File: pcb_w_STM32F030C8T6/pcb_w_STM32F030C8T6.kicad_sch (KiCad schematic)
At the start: 29 parts

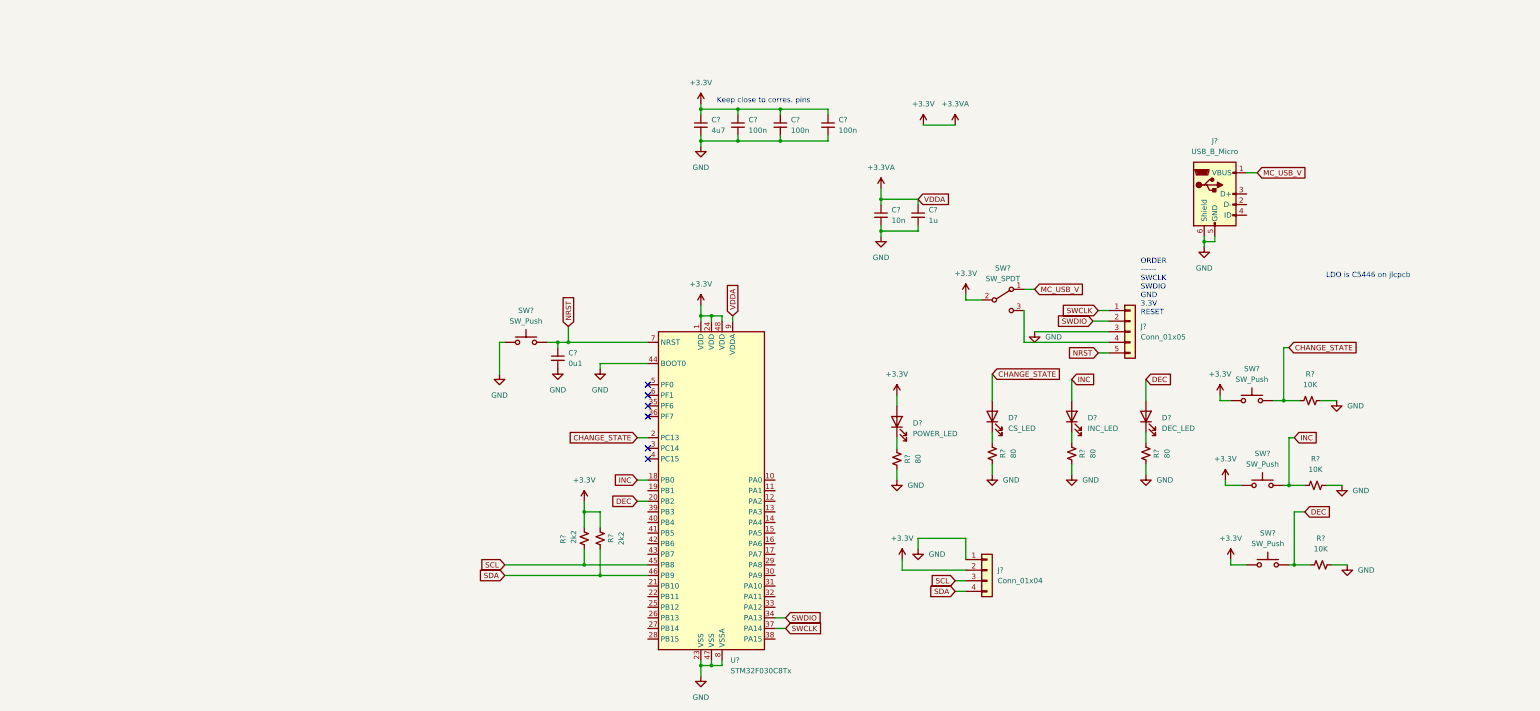
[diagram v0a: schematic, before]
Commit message: added ldo...created some footprints...and currently doing routing
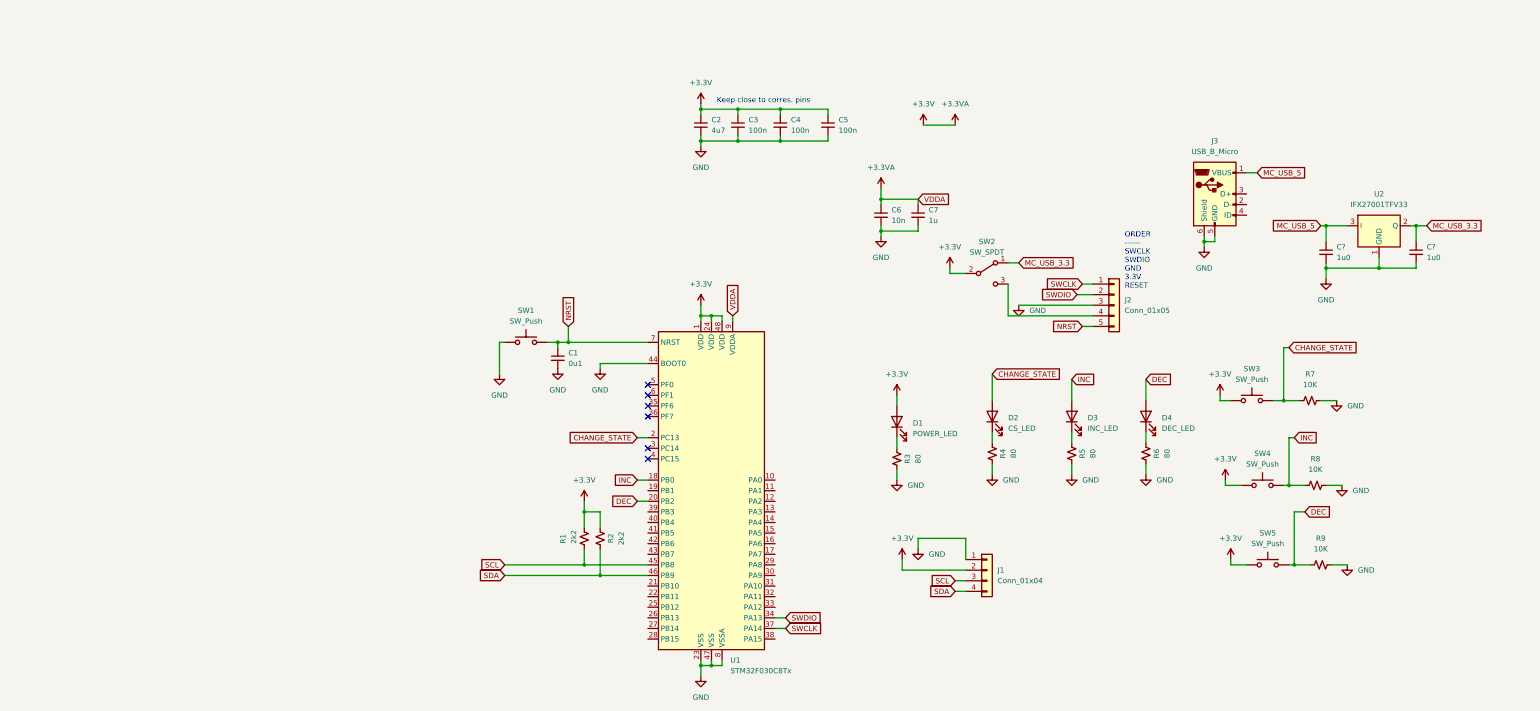
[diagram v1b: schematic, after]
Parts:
- added C? (x2): 1u0, Capacitor_SMD:C_0805_2012Metric, symbol Device:C_Small
- added U2: IFX27001TFV33, MyLibrary:SOT-23-3L, symbol Regulator_Linear:IFX27001TFV33
- J1: renamed from J?; DigiKey Part # (none) -> SSW-104-06-T-S-LL
- J2: renamed from J?; JLCPCB Part # (none) -> C124379
- SW1, SW3, SW4, SW5: renamed from SW?; footprint create one -> MyLibrary:SMD_3×4×2.0
- SW2: renamed from SW?; footprint create one -> MyLibrary:SW-SMD-JLC-C405952
- gave numbers to parts that had none: 22
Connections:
- net GND: now also C?.2, C?.2, U2.1 (GND)
- net MC_USB_V renamed MC_USB_3.3
- net MC_USB_3.3: now also C?.1, U2.2 (Q); no longer J3.1 (VBUS)
- new net MC_USB_5: C?.1, J3.1 (VBUS), U2.3 (I)
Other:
- note removed: "LDO is C5446 on jlcpcb"
- moved on the sheet: J2, SW2

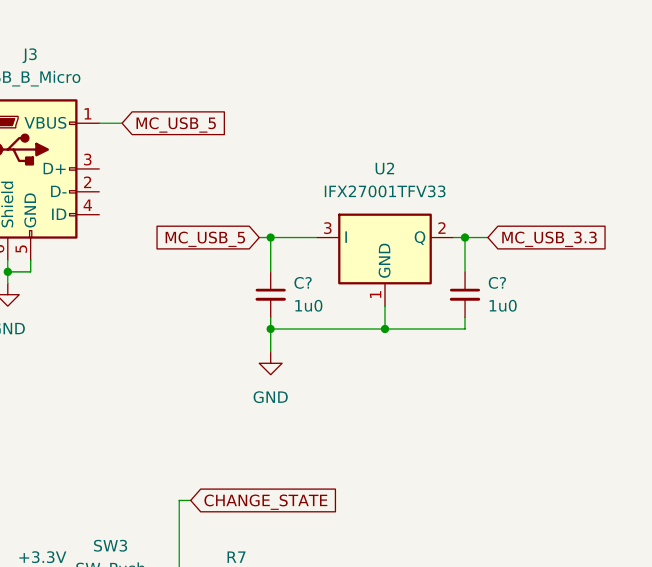
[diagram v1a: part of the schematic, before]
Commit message: made board 4 layers
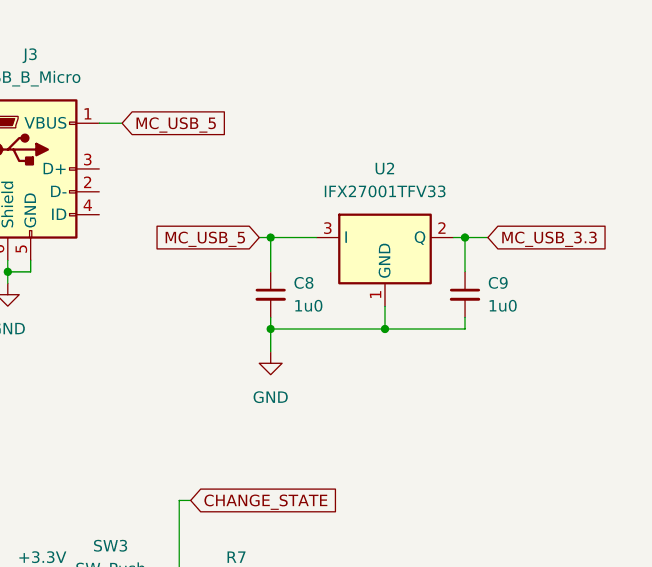
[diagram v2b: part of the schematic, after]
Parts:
- C1: footprint Capacitor_SMD:C_01005_0402Metric -> Capacitor_SMD:C_0805_2012Metric; DigiKey Part # GRM02YR60J104ME01L -> 0805ZC104KAT2A
- gave numbers to parts that had none: 2
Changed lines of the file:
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@@
       (effects (font (size 1.27 1.27)) (justify left))
     )
-    (property "Footprint" "Capacitor_SMD:C_01005_0402Metric" (id 2) (at 52.07 92.71 0)
+    (property "Footprint" "Capacitor_SMD:C_0805_2012Metric" (id 2) (at 52.07 92.71 0)
       (effects (font (size 1.27 1.27)) hide)
     )
@@
       (effects (font (size 1.27 1.27)) hide)
     )
-    (property "DigiKey Part #" "GRM02YR60J104ME01L" (id 5) (at 52.07 92.71 0)
+    (property "DigiKey Part #" "0805ZC104KAT2A" (id 5) (at 52.07 92.71 0)
       (effects (font (size 1.27 1.27)) hide)
     )
@@
   (symbol (lib_id "power:GND") (at 236.22 73.66 0) (unit 1)
     (in_bom yes) (on_board yes) (fields_autoplaced)
-    (property "Reference" "#PWR?" (id 0) (at 236.22 80.01 0)
+    (property "Reference" "#PWR0129" (id 0) (at 236.22 80.01 0)
       (effects (font (size 1.27 1.27)) hide)
     )
@@
   (symbol (lib_id "Device:C_Small") (at 257.81 67.31 0) (unit 1)
     (in_bom yes) (on_board yes) (fields_autoplaced)
-    (property "Reference" "C?" (id 0) (at 260.35 66.0462 0)
+    (property "Reference" "C9" (id 0) (at 260.35 66.0462 0)
       (effects (font (size 1.27 1.27)) (justify left))
     )
@@
   (symbol (lib_id "Device:C_Small") (at 236.22 67.31 0) (unit 1)
     (in_bom yes) (on_board yes) (fields_autoplaced)
-    (property "Reference" "C?" (id 0) (at 238.76 66.0462 0)
+    (property "Reference" "C8" (id 0) (at 238.76 66.0462 0)
       (effects (font (size 1.27 1.27)) (justify left))
     )
@@
     )
     (path "/8b6e897a-69ad-468a-b1a1-f26ad2399337"
-      (reference "#PWR?") (unit 1) (value "GND") (footprint "")
+      (reference "#PWR0129") (unit 1) (value "GND") (footprint "")
     )
     (path "/17f827b9-73cd-4aa3-8d36-45597ec3ede1"
-      (reference "C1") (unit 1) (value "0u1") (footprint "Capacitor_SMD:C_01005_0402Metric")
+      (reference "C1") (unit 1) (value "0u1") (footprint "Capacitor_SMD:C_0805_2012Metric")
     )
     (path "/ed9c3204-f848-4eeb-98bb-4c2a58dc4d9a"
@@
       (reference "C7") (unit 1) (value "1u") (footprint "Capacitor_SMD:C_0805_2012Metric")
     )
+    (path "/eadfda04-f56f-475e-9b77-9925c6870fda"
+      (reference "C8") (unit 1) (value "1u0") (footprint "Capacitor_SMD:C_0805_2012Metric")
+    )
     (path "/ad4fe0cb-eb55-43e0-b2d0-b7c510f1f6d7"
-      (reference "C?") (unit 1) (value "1u0") (footprint "Capacitor_SMD:C_0805_2012Metric")
-    )
-    (path "/eadfda04-f56f-475e-9b77-9925c6870fda"
-      (reference "C?") (unit 1) (value "1u0") (footprint "Capacitor_SMD:C_0805_2012Metric")
+      (reference "C9") (unit 1) (value "1u0") (footprint "Capacitor_SMD:C_0805_2012Metric")
     )
     (path "/e969782a-0db1-4285-870f-b759fd5a6a33"

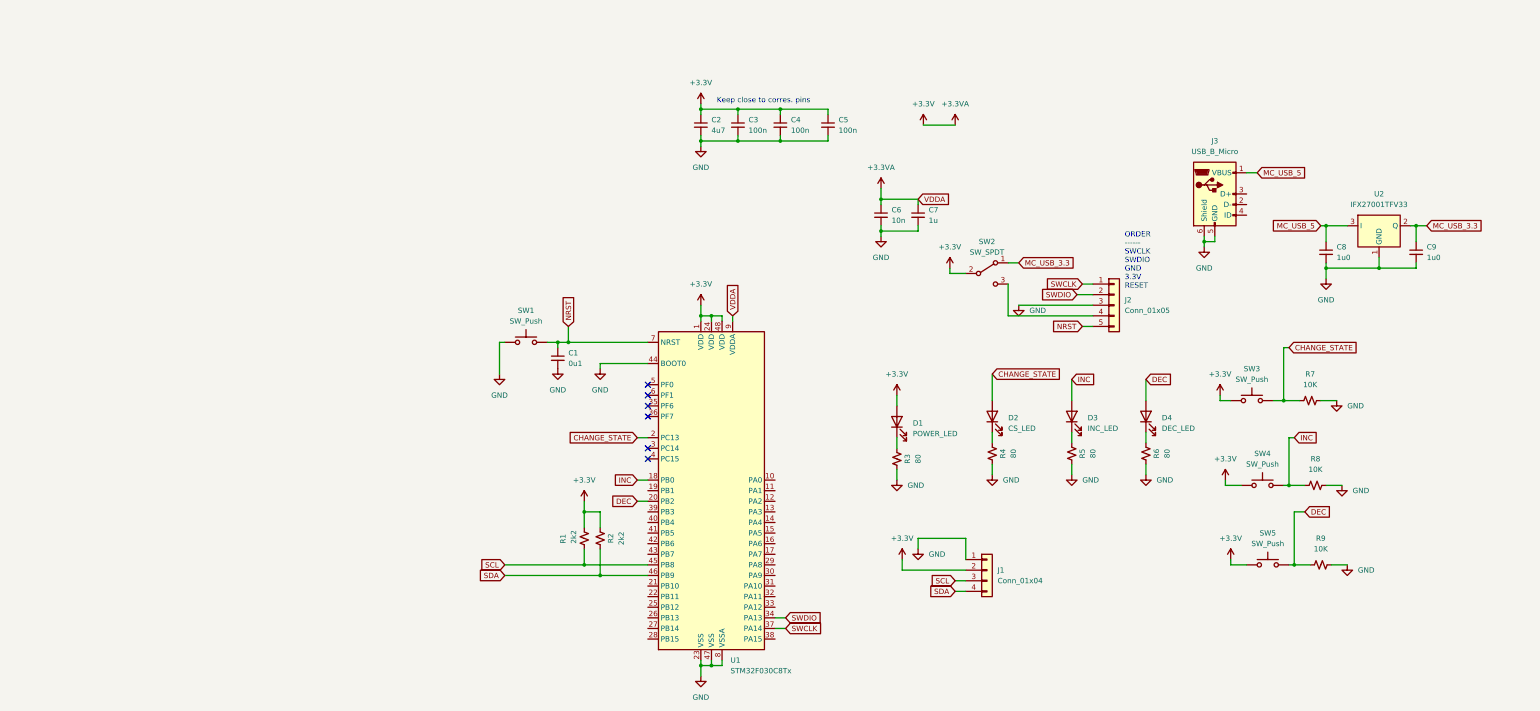
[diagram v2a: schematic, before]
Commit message: changing components and mc to ones in stock at digikey
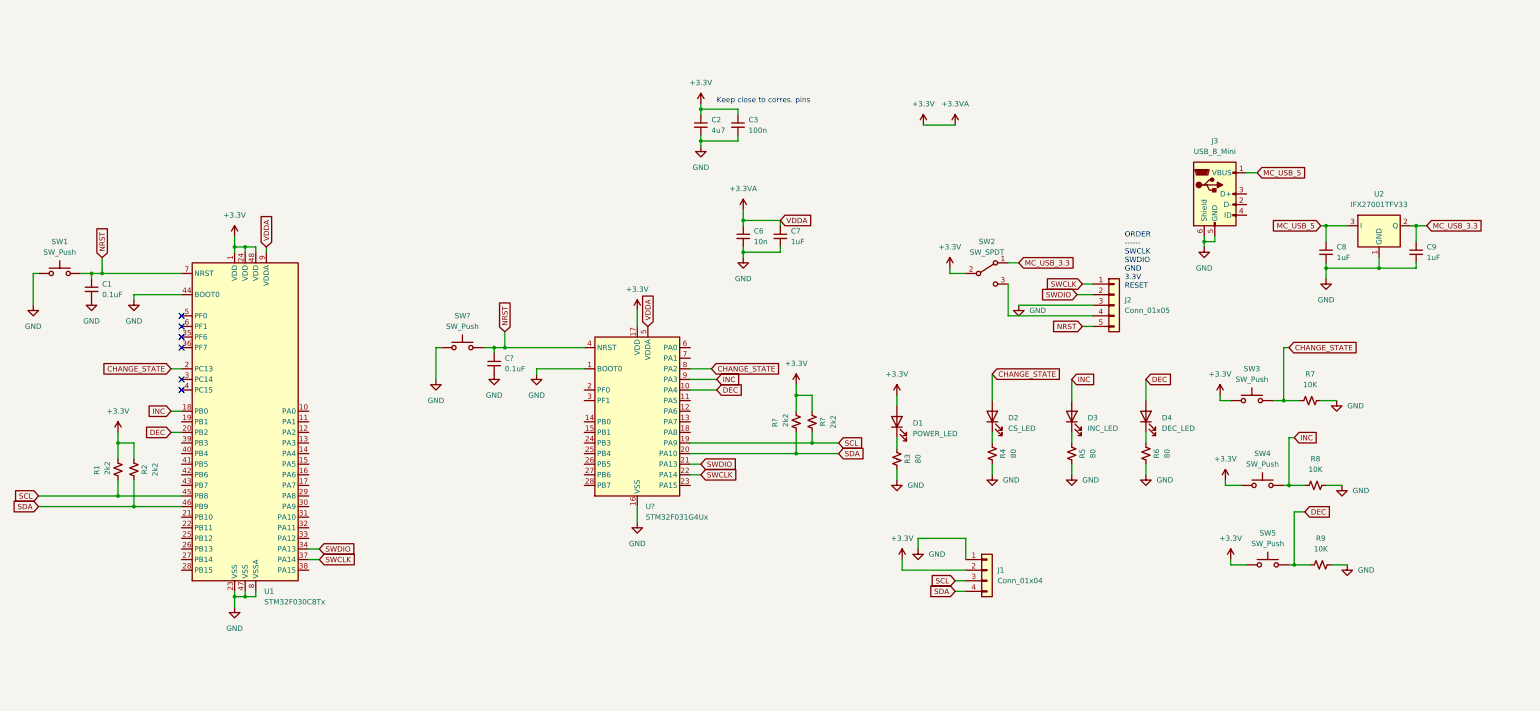
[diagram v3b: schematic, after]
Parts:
- removed C4, C5: 100n, Capacitor_SMD:C_0805_2012Metric, symbol Device:C_Small
- added C?: 0.1uF, Capacitor_SMD:C_0805_2012Metric_Pad1.18x1.45mm_HandSolder, symbol Device:C_Small
- added R? (x2): 2k2, Resistor_SMD:R_0805_2012Metric_Pad1.20x1.40mm_HandSolder, symbol Device:R_Small_US
- added SW?: SW_Push, MyLibrary:FSMSMTR-Tactile-Switch-FP, symbol Switch:SW_Push
- added U?: STM32F031G4Ux, Package_DFN_QFN:QFN-28_4x4mm_P0.5mm, symbol MCU_ST_STM32F0:STM32F031G4Ux
- C1: value 0u1 -> 0.1uF; footprint Capacitor_SMD:C_0805_2012Metric -> Capacitor_SMD:C_0805_2012Metric_Pad1.18x1.45mm_HandSolder
- C2: footprint Capacitor_SMD:C_0805_2012Metric -> Capacitor_SMD:C_0805_2012Metric_Pad1.18x1.45mm_HandSolder; DigiKey Part # (none) -> TMK212ABJ475KG-T; LCSC Part Number (none) -> C1779
- C3: footprint Capacitor_SMD:C_0805_2012Metric -> Capacitor_SMD:C_0603_1608Metric_Pad1.08x0.95mm_HandSolder; DigiKey Part # (none) -> GMC10X7R104K50NT; LCSC Part Number (none) -> C28233
- C6: footprint Capacitor_SMD:C_0805_2012Metric -> Capacitor_SMD:C_0805_2012Metric_Pad1.18x1.45mm_HandSolder; DigiKey Part # (none) -> 885342207014; LCSC Part Number (none) -> C1710
- C7: value 1u -> 1uF; footprint Capacitor_SMD:C_0805_2012Metric -> Capacitor_SMD:C_0805_2012Metric_Pad1.18x1.45mm_HandSolder; DigiKey Part # (none) -> GMC21X7R105K16NT; LCSC Part Number (none) -> C28323
- C8, C9: value 1u0 -> 1uF; footprint Capacitor_SMD:C_0805_2012Metric -> Capacitor_SMD:C_0805_2012Metric_Pad1.18x1.45mm_HandSolder; DigiKey Part # (none) -> GMC21X7R105K16NT; JLCPCB Part # C440198 -> C28323; LCSC Part Number (none) -> C28323
- D1: footprint Diode_SMD:D_0805_2012Metric -> Diode_SMD:D_0805_2012Metric_Pad1.15x1.40mm_HandSolder; DigiKey Part # (none) -> XZVG54W-1; JLCPCB Part # C84256 -> C205441; LCSC Part Number (none) -> C84256
- D2: footprint Diode_SMD:D_0805_2012Metric -> Diode_SMD:D_0805_2012Metric_Pad1.15x1.40mm_HandSolder; DigiKey Part # (none) -> XZVG54W-1; LCSC Part Number (none) -> C205441
- D3: footprint Diode_SMD:D_0805_2012Metric -> Diode_SMD:D_0805_2012Metric_Pad1.15x1.40mm_HandSolder; DigiKey Part # (none) -> XZVG54W-1; JLCPCB Part # C188728 -> C205441; LCSC Part Number (none) -> C389524
- D4: footprint Diode_SMD:D_0805_2012Metric -> Diode_SMD:D_0805_2012Metric_Pad1.15x1.40mm_HandSolder; DigiKey Part # (none) -> XZVG54W-1; JLCPCB Part # C397047 -> C205441; LCSC Part Number (none) -> C397047
- J1: DigiKey Part # SSW-104-06-T-S-LL -> SQT-105-01-F-S-RA-001
- J2: LCSC Part Number (none) -> C124379
- J3: value USB_B_Micro -> USB_B_Mini; DigiKey Part # KMBX-SMT5S-S30TRMT -> 0548191572; JLCPCB Part # (none) -> C91144; LCSC Part Number (none) -> C91144
- R1, R2: footprint Resistor_SMD:R_0805_2012Metric -> Resistor_SMD:R_0805_2012Metric_Pad1.20x1.40mm_HandSolder; DigiKey Part # (none) -> AC0805FR-102K2L; LCSC Part Number (none) -> C17520
- R3, R4, R5, R6: footprint Resistor_SMD:R_1206_3216Metric -> Resistor_SMD:R_0805_2012Metric_Pad1.20x1.40mm_HandSolder; DigiKey Part # (none) -> ERA-6AEB80R6V; JLCPCB Part # C966395 -> C109433; LCSC Part Number (none) -> C109433
- R7, R8, R9: footprint Resistor_SMD:R_0805_2012Metric -> Resistor_SMD:R_0805_2012Metric_Pad1.20x1.40mm_HandSolder; DigiKey Part # (none) -> RN10F1002CT5-50; LCSC Part Number (none) -> C17414
- SW1, SW3, SW4, SW5: footprint MyLibrary:SMD_3×4×2.0 -> MyLibrary:FSMSMTR-Tactile-Switch-FP; DigiKey Part # (none) -> FSMSMTR; LCSC Part Number (none) -> C720477
- SW2: footprint MyLibrary:SW-SMD-JLC-C405952 -> MyLibrary:CL-SB-22A-01T-Slide-Switch-FP; DigiKey Part # (none) -> CL-SB-22A-01T; LCSC Part Number (none) -> C405952
- U1: DigiKey Part # (none) -> 497-13619-ND; LCSC Part Number (none) -> C23922
- U2: footprint MyLibrary:SOT-23-3L -> MyLibrary:SOT23F; DigiKey Part # (none) -> ZXTR2105FFQ-7; LCSC Part Number (none) -> C5446
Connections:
- net +3.3VA: now also R?.2, R?.2, U?.17 (VDD), U?.5 (VDDA)
- net CHANGE_STATE: now also U?.8 (PA2)
- net DEC: now also U?.10 (PA4)
- net GND: now also C?.2, SW?.1, U?.1 (BOOT0), U?.16 (VSS)
- net INC: now also U?.9 (PA3)
- net NRST: now also C?.1, SW?.2, U?.4 (NRST)
- net SCL: now also R?.1, U?.19 (PA9)
- net SDA: now also R?.1, U?.20 (PA10)
- net SWCLK: now also U?.22 (PA14)
- net SWDIO: now also U?.21 (PA13)
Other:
- moved on the sheet: C1, C6, C7, R1, R2, SW1, U1
